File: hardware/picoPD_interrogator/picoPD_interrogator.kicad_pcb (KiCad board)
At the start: 2 copper layers, 66 x 25.7 mm, 29 parts, among them Q1 rohm-RE1C002UN, Q2 rohm-RE1C002UN, Q3 rohm-RE1C002UN, Q4 rohm-RE1C002UN, U2 ST-LM393QT

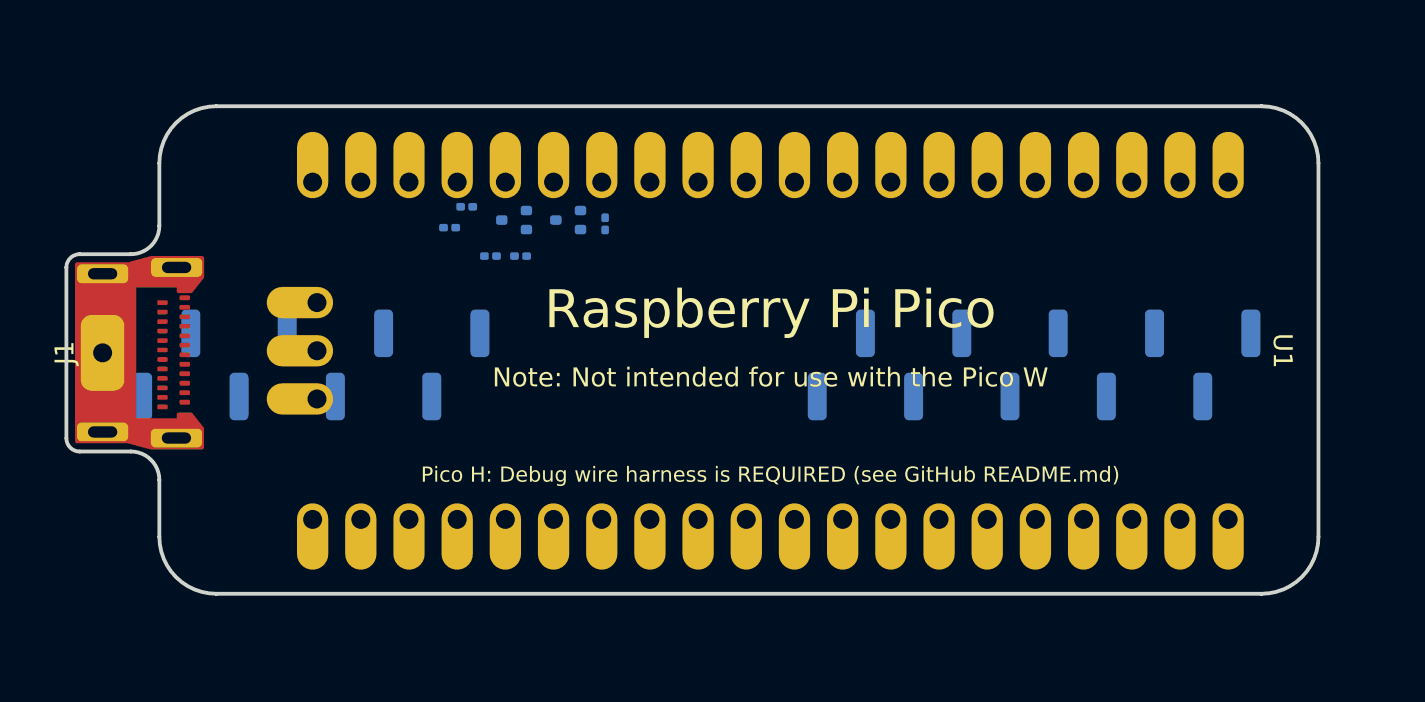
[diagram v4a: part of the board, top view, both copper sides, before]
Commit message: Added 3.3v fill on the F.Cu layer.
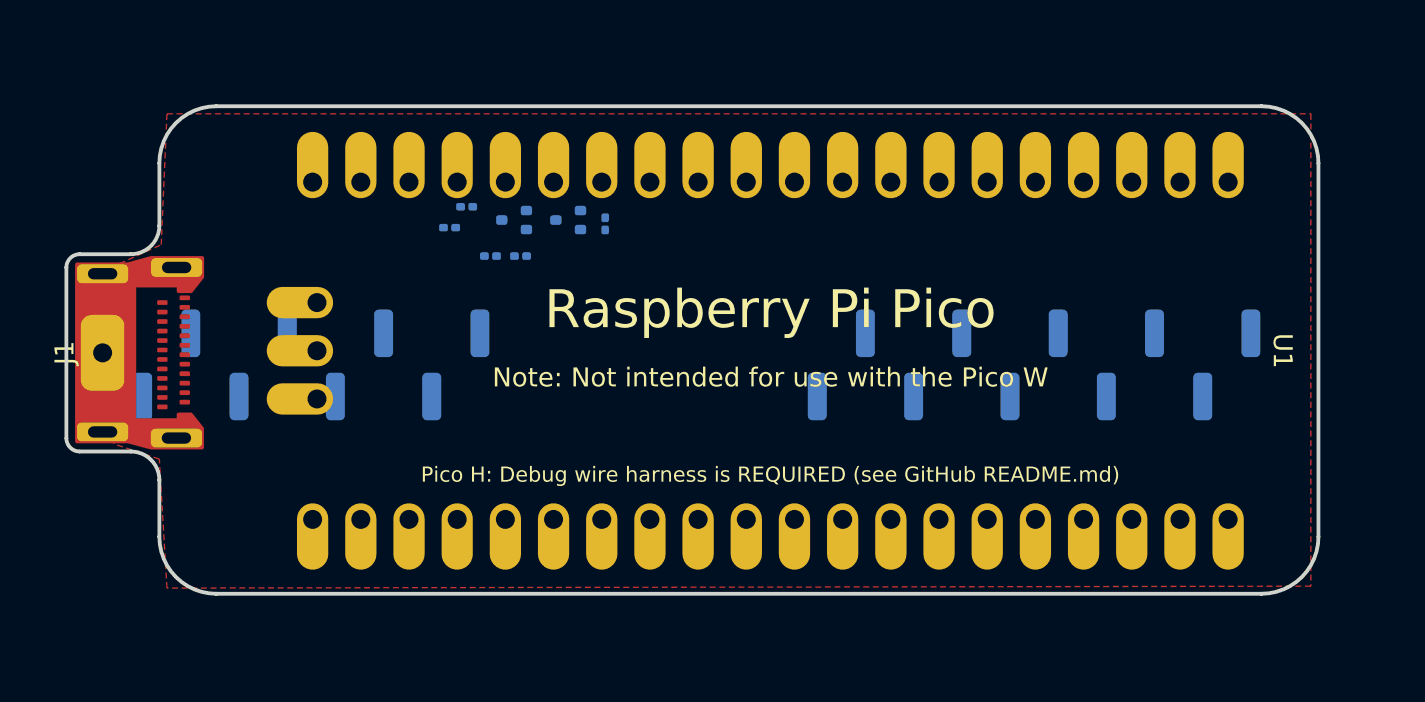
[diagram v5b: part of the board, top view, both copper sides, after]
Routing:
- added copper zone on F.Cu, net /3V3
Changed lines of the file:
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@@
 		(tags "resistor")
 		(property "Reference" "R12"
-			(at 0 1.05 270)
+			(at 0 1.05 -90)
 			(layer "B.SilkS")
 			(effects
@@
 		)
 		(property "Value" "100R"
-			(at 0 -1.05 270)
+			(at 0 -1.05 -90)
 			(layer "B.Fab")
 			(effects
@@
 		)
 		(fp_text user "${REFERENCE}"
-			(at 0 0.68 270)
+			(at 0 0.68 -90)
 			(layer "B.Fab")
 			(effects
@@
 		(tags "resistor")
 		(property "Reference" "R11"
-			(at 0 1.05 360)
+			(at 0 1.05 0)
 			(layer "B.SilkS")
 			(effects
@@
 		)
 		(property "Value" "?"
-			(at 0 -1.05 360)
+			(at 0 -1.05 0)
 			(layer "B.Fab")
 			(effects
@@
 		)
 		(fp_text user "${REFERENCE}"
-			(at 0 0.68 360)
+			(at 0 0.68 0)
 			(layer "B.Fab")
 			(effects
@@
 		(layer "User.1")
 	)
+	(zone
+		(net 32)
+		(net_name "/3V3")
+		(layer "F.Cu")
+		(hatch edge 0.5)
+		(connect_pads
+			(clearance 0.5)
+		)
+		(min_thickness 0.25)
+		(filled_areas_thickness no)
+		(fill yes
+			(thermal_gap 0.5)
+			(thermal_bridge_width 0.5)
+		)
+		(polygon
+			(pts
+				(xy 125.3 75.4) (xy 185.6 75.4) (xy 185.6 100.3) (xy 125.3 100.4) (xy 124.9 93.6) (xy 122.5 92.8)
+				(xy 122.8 83.3) (xy 125 82.3)
+			)
+		)
+	)
 )

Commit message: Placing components... Also added the B.Cu GND layer fill.
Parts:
- moved C1 71.1 mm to (169.5, 57.6)
- moved R1 71.1 mm to (169.5, 61.1)
- moved R2 71.1 mm to (169.5, 62.9)
- moved R3 71.1 mm to (169.5, 64.6)
- moved R4 71.1 mm to (169.5, 66.3)
- moved U2 71.1 mm to (161.1, 58.7)
- moved R10 71.1 mm to (167.0, 66.3)
- moved R5 71.1 mm to (167.0, 57.6)
- moved R6 71.1 mm to (167.0, 59.4)
- moved R7 71.1 mm to (167.0, 61.1)
- moved R8 71.1 mm to (167.0, 62.9)
- moved Q1 27.3 mm to (152.4, 81.0), turned to 0 degrees
- moved Q2 24.0 mm to (155.3, 81.0), turned to 0 degrees
- moved R12 0.66 mm to (148.4, 80.5)
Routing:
- added copper zone on B.Cu, net GND

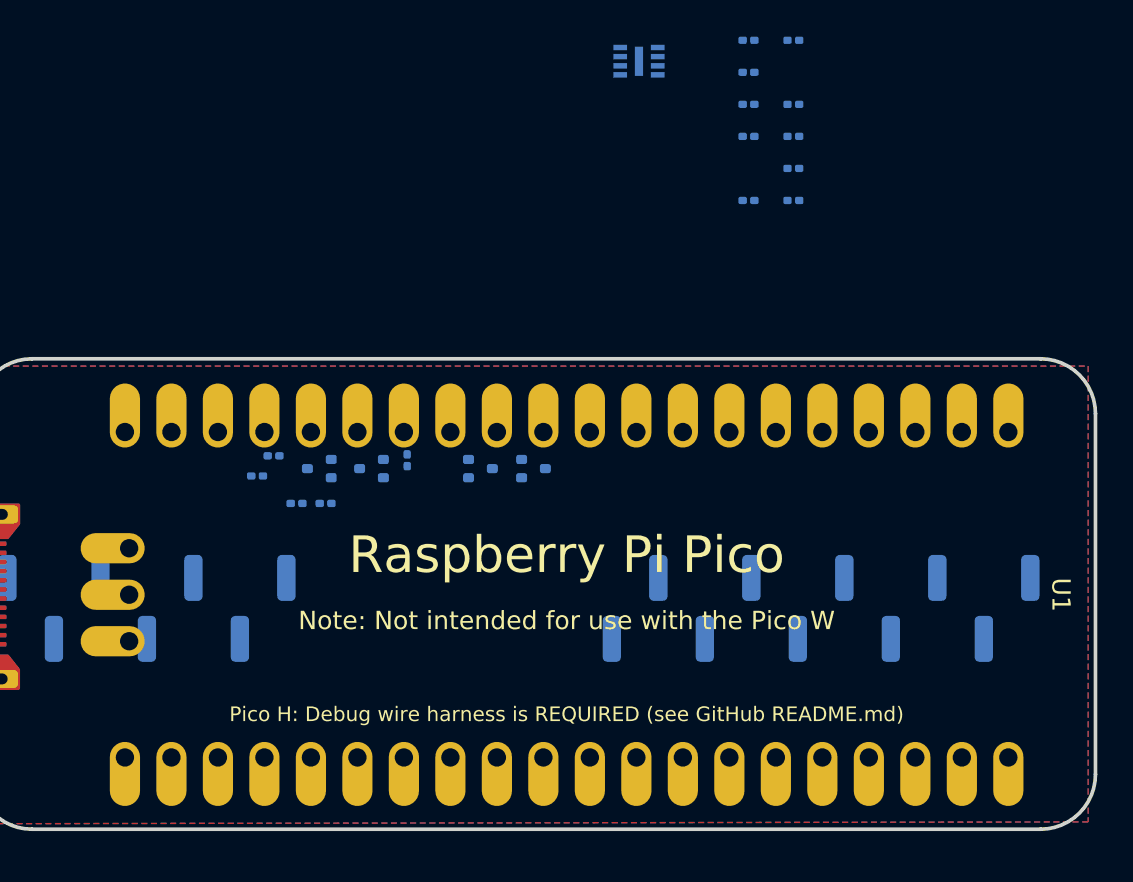
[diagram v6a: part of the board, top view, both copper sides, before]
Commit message: Added additional pads to the underside of the RaspberryPiFoundation Pico Footprint.
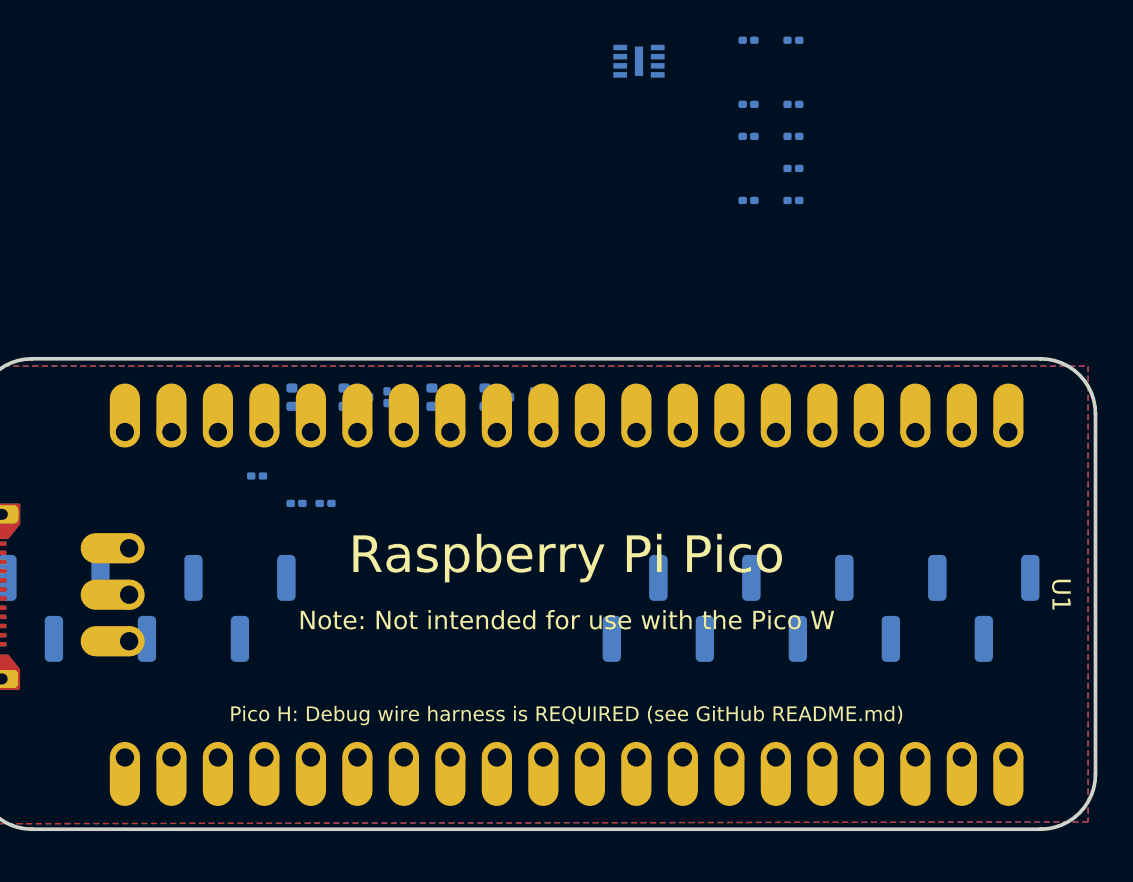
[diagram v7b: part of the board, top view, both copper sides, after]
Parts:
- moved R6 21.3 mm to (155.3, 77.1), turned to 90 degrees
- moved R12 8.34 mm to (140.8, 77.1), turned to -90 degrees
- moved R9 6.98 mm to (147.3, 77.1), turned to -90 degrees
- moved Q4 5.38 mm to (142.8, 77.1), turned to 0 degrees
- moved Q1 4.38 mm to (150.4, 77.1)
- moved Q2 4.38 mm to (153.3, 77.1)
- moved Q3 4.38 mm to (145.6, 77.1), turned to 0 degrees

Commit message: Working on PCB route.
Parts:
- moved R1 39.1 mm to (150.0, 95.0), turned to 90 degrees
- moved U2 36.4 mm to (153.2, 94.2)
- moved R2 36.4 mm to (150.0, 93.5), turned to 90 degrees
- moved R3 33.6 mm to (155.8, 95.2)
- moved C1 30.2 mm to (150.0, 80.7)
- moved R5 24.7 mm to (158.9, 81.0), turned to 0 degrees
- moved R7 24.3 mm to (148.7, 77.1), turned to 90 degrees
- moved R8 23.7 mm to (151.5, 80.7), turned to 0 degrees
- moved R10 21.7 mm to (151.5, 81.5)
- moved R4 17.2 mm to (160.4, 81.0)
- moved R13 3.70 mm to (143.9, 81.5)
- moved C2 2.20 mm to (142.4, 80.7)
- moved R11 2.20 mm to (143.9, 80.7)
- moved R6 0.30 mm to (155.0, 77.1)
- moved R12 0.20 mm to (141.0, 77.1)
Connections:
- U1 pad 10: unconnected-(U1-GP7-Pad10) -> /CC2_RX
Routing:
- net GND: track 0.00 -> 106.4 mm
- net /SWD_CLK: track 0.00 -> 36.7 mm, vias 0 -> 1
- net /SWD_IO: track 0.00 -> 30.1 mm, vias 0 -> 1
- net Net-(J2-C1): track 0.00 -> 21.9 mm, vias 0 -> 2
- net /CC2_RX: track 0.00 -> 20.5 mm, vias 0 -> 2
- net /CC1_RX: track 0.00 -> 18.2 mm, vias 0 -> 2
- net /RP2_TO_FLIP: track 0.00 -> 17.3 mm
- net /BMC_VREF: track 0.00 -> 15.8 mm, vias 0 -> 2
- net /FLIP_TO_RP2: track 0.00 -> 14.3 mm
- net /CC2_CONN: track 0.00 -> 12.2 mm, vias 0 -> 1
- net /3V3: track 0.00 -> 9.42 mm, vias 0 -> 5
- net /CC1_TX: track 0.00 -> 6.56 mm
- net /CC2_TX: track 0.00 -> 6.51 mm
- net /CC1_TX_L: track 0.00 -> 2.11 mm
- net /CC2_TX_L: track 0.00 -> 1.83 mm
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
